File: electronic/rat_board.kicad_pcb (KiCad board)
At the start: 2 copper layers, 43.2 x 48.3 mm, 51 parts, among them SW1 SW_PUSH_SMALL_H, SW2 SWITCH_INV, SW3 SELECT_BUTTON, SW4 START_BUTTON

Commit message: added graphics on PCB
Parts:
- added G***: LOGO, LOGO, B.Cu at (57.0, 44.7)
- added G***: LOGO, LOGO, B.Cu at (72.8, 58.7)

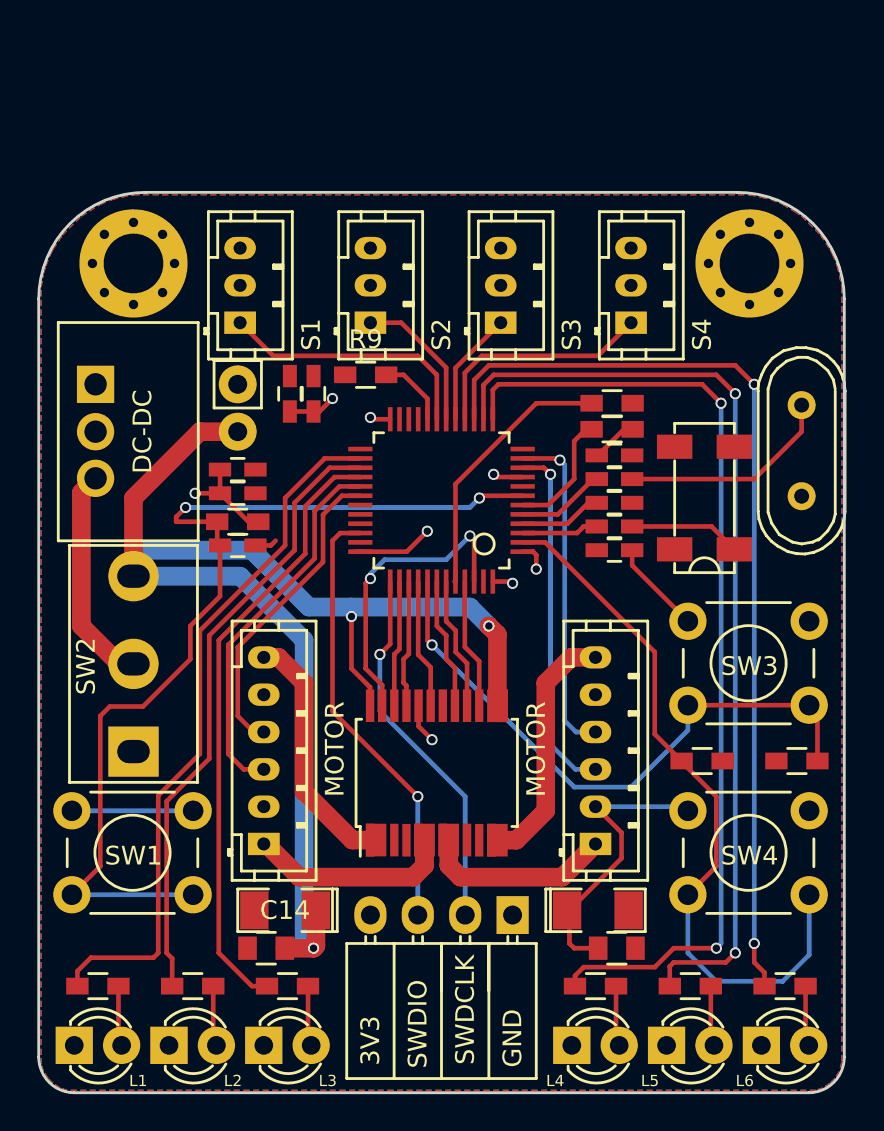
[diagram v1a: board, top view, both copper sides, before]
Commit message: logos and filled zones
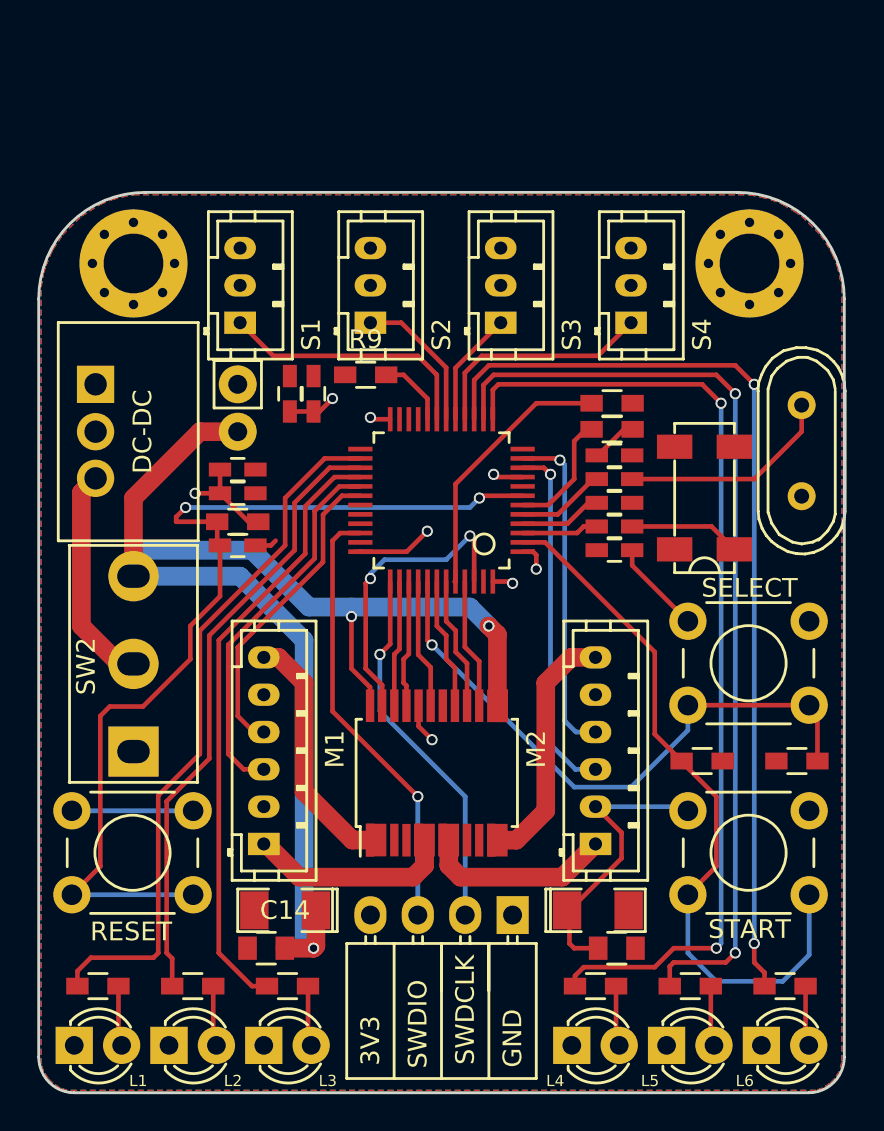
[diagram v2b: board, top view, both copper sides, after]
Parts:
- renumbered MOTOR to M1, MOTOR to M2, SW1 to RESET, SW3 to SELECT, SW4 to START
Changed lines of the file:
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@@
     (visible_elements FFFEFF7F)
     (pcbplotparams
-      (layerselection 0x00030_80000001)
+      (layerselection 0x010f0_80000001)
       (usegerberextensions false)
       (excludeedgelayer true)
@@
       (outputformat 1)
       (mirror false)
-      (drillshape 1)
+      (drillshape 0)
       (scaleselection 1)
       (outputdirectory ""))
@@
     (descr https://www.omron.com/ecb/products/pdf/en-b3f.pdf)
     (tags "tact sw push 6mm")
-    (fp_text reference SW1 (at 3.302 2.413) (layer F.SilkS)
+    (fp_text reference RESET (at 3.175 6.477) (layer F.SilkS)
       (effects (font (size 1 1) (thickness 0.15)))
     )
@@
     (descr https://www.omron.com/ecb/products/pdf/en-b3f.pdf)
     (tags "tact sw push 6mm")
-    (fp_text reference SW3 (at 3.302 2.413) (layer F.SilkS)
+    (fp_text reference SELECT (at 3.302 -1.778) (layer F.SilkS)
       (effects (font (size 1 1) (thickness 0.15)))
     )
@@
     (descr https://www.omron.com/ecb/products/pdf/en-b3f.pdf)
     (tags "tact sw push 6mm")
-    (fp_text reference SW4 (at 3.302 2.413) (layer F.SilkS)
+    (fp_text reference START (at 3.302 6.35) (layer F.SilkS)
       (effects (font (size 1 1) (thickness 0.15)))
     )
@@
     (descr http://www.jst-mfg.com/product/pdf/eng/ePH.pdf)
     (tags "connector jst ph")
-    (fp_text reference MOTOR (at 5.08 3.81 90) (layer F.SilkS)
+    (fp_text reference M1 (at 5.08 3.81 90) (layer F.SilkS)
       (effects (font (size 1 1) (thickness 0.15)))
     )
@@
     (descr http://www.jst-mfg.com/product/pdf/eng/ePH.pdf)
     (tags "connector jst ph")
-    (fp_text reference MOTOR (at 5.08 -3.175 90) (layer F.SilkS)
-      (effects (font (size 1 1) (thickness 0.15)))
-    )
+    (fp_text reference M2 (at 5.08 -3.175 90) (layer F.SilkS)
+      (effects (font (size 1 1) (thickness 0.15)))
+    )

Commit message: added an additional uart connector
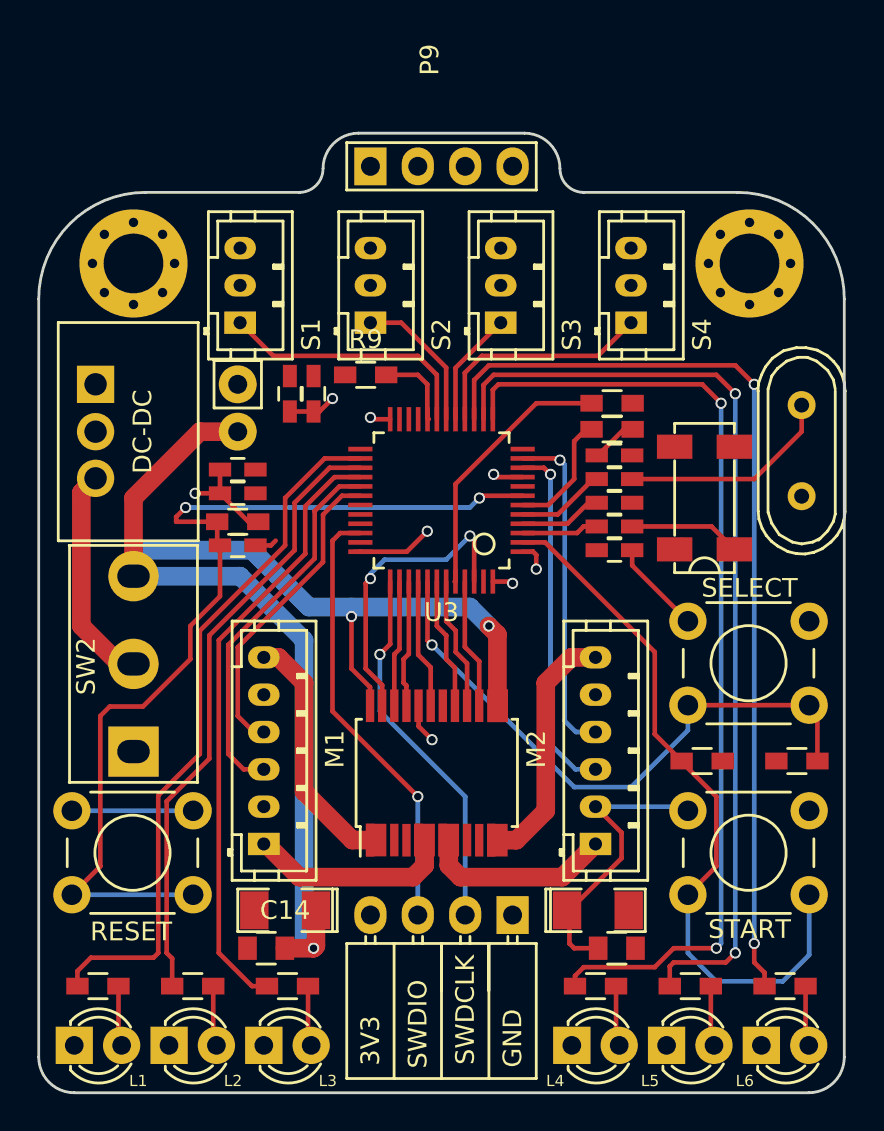
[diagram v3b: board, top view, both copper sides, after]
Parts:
- added P9: CONN_01X04, Pin_Headers:Pin_Header_Straight_1x04, F.Cu at (52.8, 27.7)
- moved G*** 59.6 mm to (3.05, 19.4)
- gave numbers to parts that had none: 1
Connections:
- U3 pad 21: Net-(U3-Pad21) -> /TX3
- U3 pad 22: Net-(U3-Pad22) -> /RX3
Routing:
- net /BOOT1: track 3.84 -> 4.36 mm
- removed copper zone on B.Cu, net +3V3
- removed copper zone on F.Cu, net GND
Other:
- board size 43.2 x 48.3 mm -> 43.2 x 51.4 mm

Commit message: small update
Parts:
- removed the G*** at (72.8, 58.7)
- SW2: footprint Connect:Wafer_Vertical10x5.8x7RM2.5-3 -> Buttons_Switches_ThroughHole:SW_PUSH_x2
- moved G*** 58.9 mm to (56.1, 45.0)
- moved SW2 3.78 mm to (42.9, 56.9)
- moved S4 1.78 mm to (65.0, 36.1)
- moved ? 1.27 mm to (38.1, 43.2)
- moved S1 1.27 mm to (47.1, 36.1)
- moved ? 1.02 mm to (41.1, 33.0)
- moved ? 1.02 mm to (72.1, 33.0)
- moved S3 0.76 mm to (59.1, 36.1)
- moved S2 0.25 mm to (53.1, 36.1)
- renumbered P9 to ?, R9 to ?
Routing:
- net /TX3: track 0.00 -> 16.6 mm, vias 0 -> 1
- net /RX3: track 0.00 -> 15.3 mm, vias 0 -> 1
- net Net-(SW2-Pad2): track 11.9 -> 3.59 mm
- net /RESET: track 52.9 -> 45.2 mm
- net +BATT: track 74.7 -> 67.4 mm
- net /IR4: track 12.5 -> 10.7 mm
- net /IR1: track 14.1 -> 12.8 mm
- added copper zone on B.Cu, net +3V3
- added copper zone on F.Cu, net GND

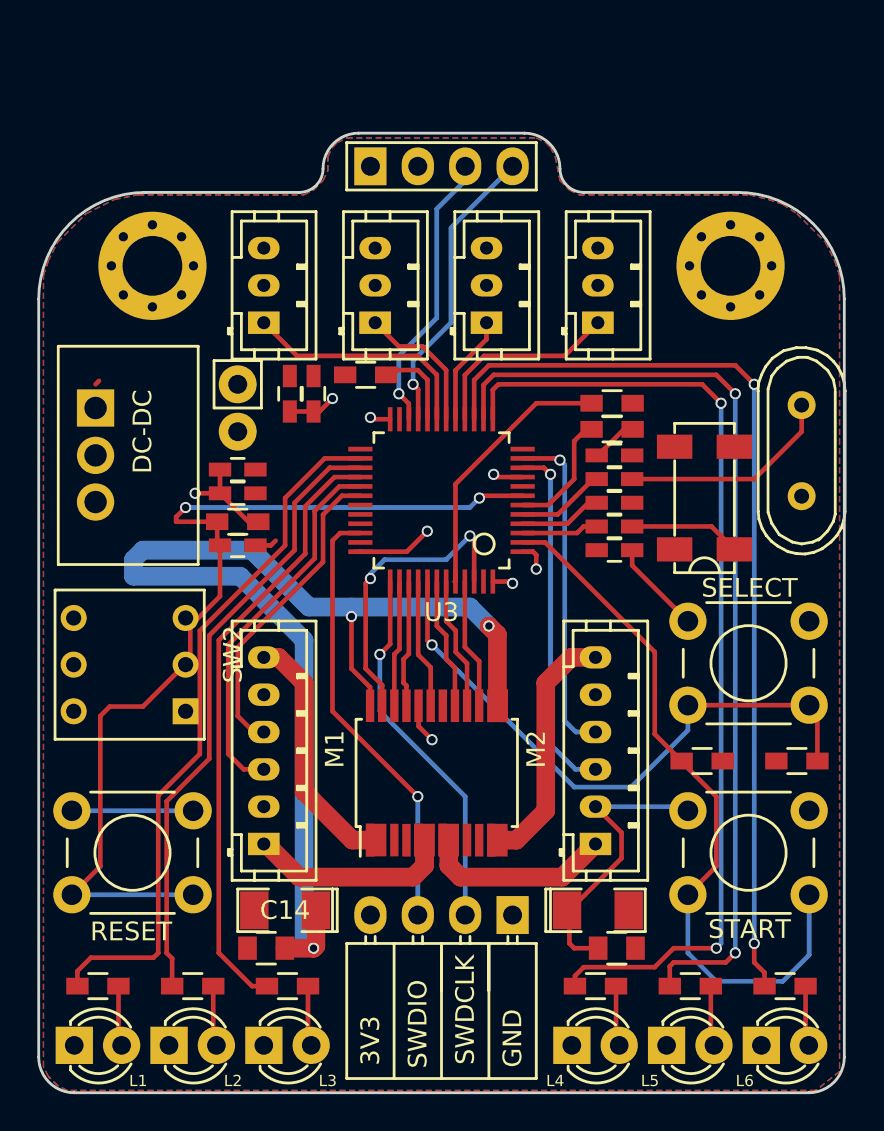
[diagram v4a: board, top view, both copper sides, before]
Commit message: smaller pushbutton on pcb
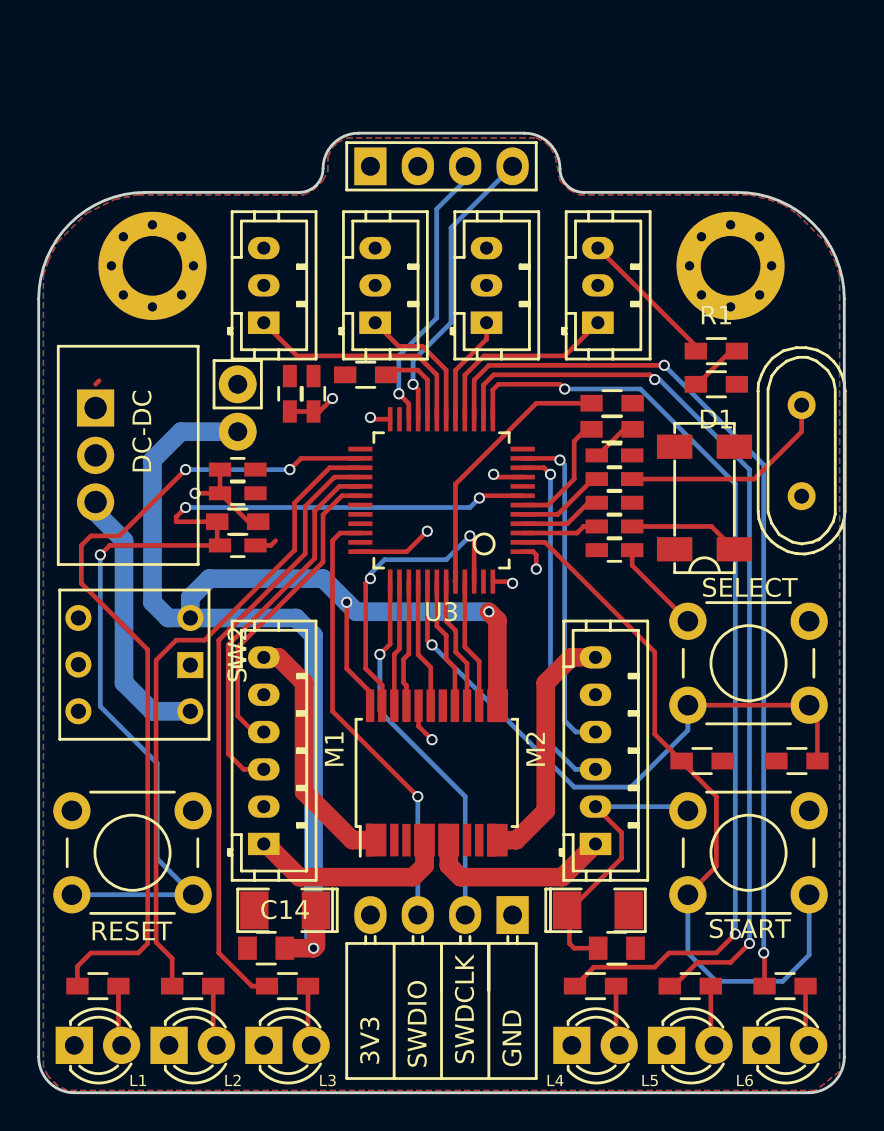
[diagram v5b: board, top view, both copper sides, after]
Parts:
- added D1: LED_Power, Resistors_SMD:R_0603_HandSoldering, F.Cu at (71.4, 39.4)
- added R1: 100, Resistors_SMD:R_0603_HandSoldering, F.Cu at (71.4, 37.6)
- moved SW2 0.25 mm to (43.2, 56.9)
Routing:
- net /RESET: track 45.2 -> 56.7 mm, vias 2 -> 3
- net Net-(SW2-Pad2): track 3.59 -> 14.5 mm
- net +3V3: track 41.0 -> 48.7 mm
- net /LED0: track 37.7 -> 45.1 mm, vias 0 -> 2
- net GND: track 8.00 -> 1.50 mm
- net +BATT: track 67.4 -> 72.1 mm
- net Net-(D1-Pad2): track 0.00 -> 2.94 mm
- net /LED5: track 50.3 -> 48.1 mm
- net /LED4: track 50.8 -> 49.0 mm
- net /LED3: track 52.4 -> 50.8 mm
- net /LED1: track 33.8 -> 34.5 mm

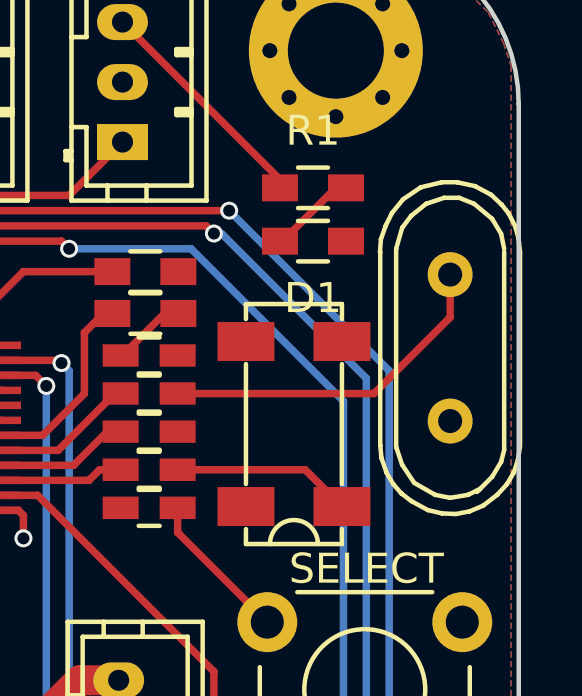
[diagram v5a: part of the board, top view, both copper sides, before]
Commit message: component values on board
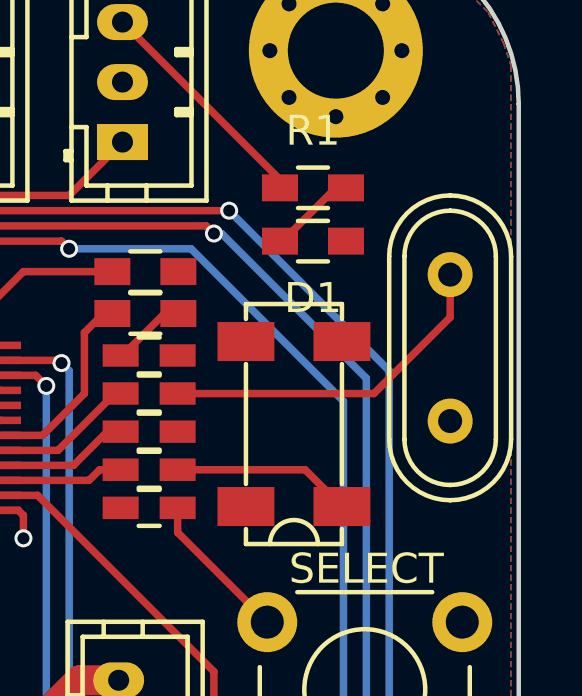
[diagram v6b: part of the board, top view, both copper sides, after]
